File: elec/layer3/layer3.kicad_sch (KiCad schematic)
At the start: 46 parts, among them U1 CD74HC4067SM, U2 CD74HC4067SM, U3 TEENSY40, U4 4754, U5 113991054

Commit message: l3 almost done
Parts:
- removed U3: TEENSY40, layer2-pcb-footprints:TEENSY40, symbol layer2-pcb-symbols:TEENSY40
- added H1, H2, H3, H4: MountingHole, MountingHole:MountingHole_3.2mm_M3_DIN965_Pad, symbol Mechanical:MountingHole
- added J10, J4: Conn_01x05, Connector_JST:JST_XH_B5B-XH-A_1x05_P2.50mm_Vertical, symbol Connector_Generic:Conn_01x05
- added J8, J9: XT30PW-M, L3:AMASS_XT30PW-M, symbol layer1-pcb-symbols:XT30PW-M
- U1, U2: footprint CD74HC4067SM96G4:SOP65P780X200-24N -> L3:CD74HC4067SM
- U4: footprint IMU:MODULE_4754 -> L3:MODULE_4754
- U5: footprint Layer1_Symbol_Footprints:XiaoSeeedStudioEsp32 -> L3:XiaoSeeedStudioEsp32
- U6: footprint OPENMVM7V2:OPENMV_M7 -> L3:OPENMV_M7
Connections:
- net +3V3: now also J9.P
- net +5V: now also J8.P
- net GND: now also J10.5 (Pin_5), J4.5 (Pin_5), J8.N, J9.N
- net Mux Com (17-32): now also U5.1 (D0), U5.6 (D5)
- net RX (CAM): now also J4.3 (Pin_3)
- net RX(ESP32): now also J4.1 (Pin_1)
- net S0: now also U5.2 (D1)
- net S1: now also U5.3 (D2)
- net S2: now also U5.4 (D3)
- net S3: now also U5.5 (D4)
- net TX (CAM): now also J4.4 (Pin_4)
- net TX(ESP32): now also J4.2 (Pin_2)
- net RX(IMU) renamed SCL (IMU)
- net SCL (IMU): now also J10.1 (Pin_1)
- net TX(IMU) renamed SDA (IMU)
- net SDA (IMU): now also J10.2 (Pin_2)
- no-connect marks 50 -> 24

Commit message: l3 done
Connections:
- net Mux Com (17-32): no longer R33.2, U2.1 (COM), U5.6 (D5)
- new net Mux Com (1-16): R33.2, U2.1 (COM), U5.6 (D5)

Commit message: l3 touched
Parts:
- removed IR31, IR32: TSSP58038, OptoDevice:Vishay_MINICAST-3Pin, symbol Sensor_Proximity:TSSP58038
- added SW1, SW2, SW3, SW4: SW_SPDT_312, L3:SS12D00G3, symbol Switch:SW_SPDT_312
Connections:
- net IR31 is gone; now on net IR30: U1.17 (I14)
- net +3V3: now also SW1.3 (A), SW2.3 (A), SW3.3 (A), SW4.3 (A)
- net GND: now also SW1.2 (C), SW2.2 (C), SW3.2 (C), SW4.2 (C)
- net IR16: now also U1.9 (I0); no longer U2.16 (I15)
- net IR17: now also U1.8 (I1); no longer U1.9 (I0)
- net IR18: now also U1.7 (I2); no longer U1.8 (I1)
- net IR19: now also U1.6 (I3); no longer U1.7 (I2)
- net IR20: now also U1.5 (I4); no longer U1.6 (I3)
- net IR21: now also U1.4 (I5); no longer U1.5 (I4)
- net IR22: now also U1.3 (I6); no longer U1.4 (I5)
- net IR23: now also U1.2 (I7); no longer U1.3 (I6)
- net IR24: now also U1.23 (I8); no longer U1.2 (I7)
- net IR25: now also U1.22 (I9); no longer U1.23 (I8)
- net IR26: now also U1.21 (I10); no longer U1.22 (I9)
- net IR27: now also U1.20 (I11); no longer U1.21 (I10)
- net IR28: now also U1.19 (I12); no longer U1.20 (I11)
- net IR29: now also U1.18 (I13); no longer U1.19 (I12)
- net IR30: no longer U1.18 (I13)
- net Strat4: now reaches U5.10 (D9)
- net Strat4: now also SW4.1 (B)
- net Strat3: now reaches U5.9 (D8)
- net Strat3: now also SW3.1 (B)
- net IR32 renamed Strat2
- net Strat2: now also SW2.1 (B)
- new net Strat1: SW1.1 (B), U2.16 (I15)
- no-connect marks 24 -> 22

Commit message: l3 : edited schematics
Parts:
- removed IR15, IR30: TSSP58038, OptoDevice:Vishay_MINICAST-3Pin, symbol Sensor_Proximity:TSSP58038
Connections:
- net IR15 is gone; now on net Strat1: U2.17 (I14)
- net IR30 is gone; now on net Strat3: U1.17 (I14)
- net Strat1: no longer U2.16 (I15)
- net Strat2: now also U2.16 (I15); no longer U1.16 (I15)
- net Strat3: no longer U5.9 (D8)
- net Strat4: now also U1.16 (I15); no longer U5.10 (D9)
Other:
- moved on the sheet: IR29

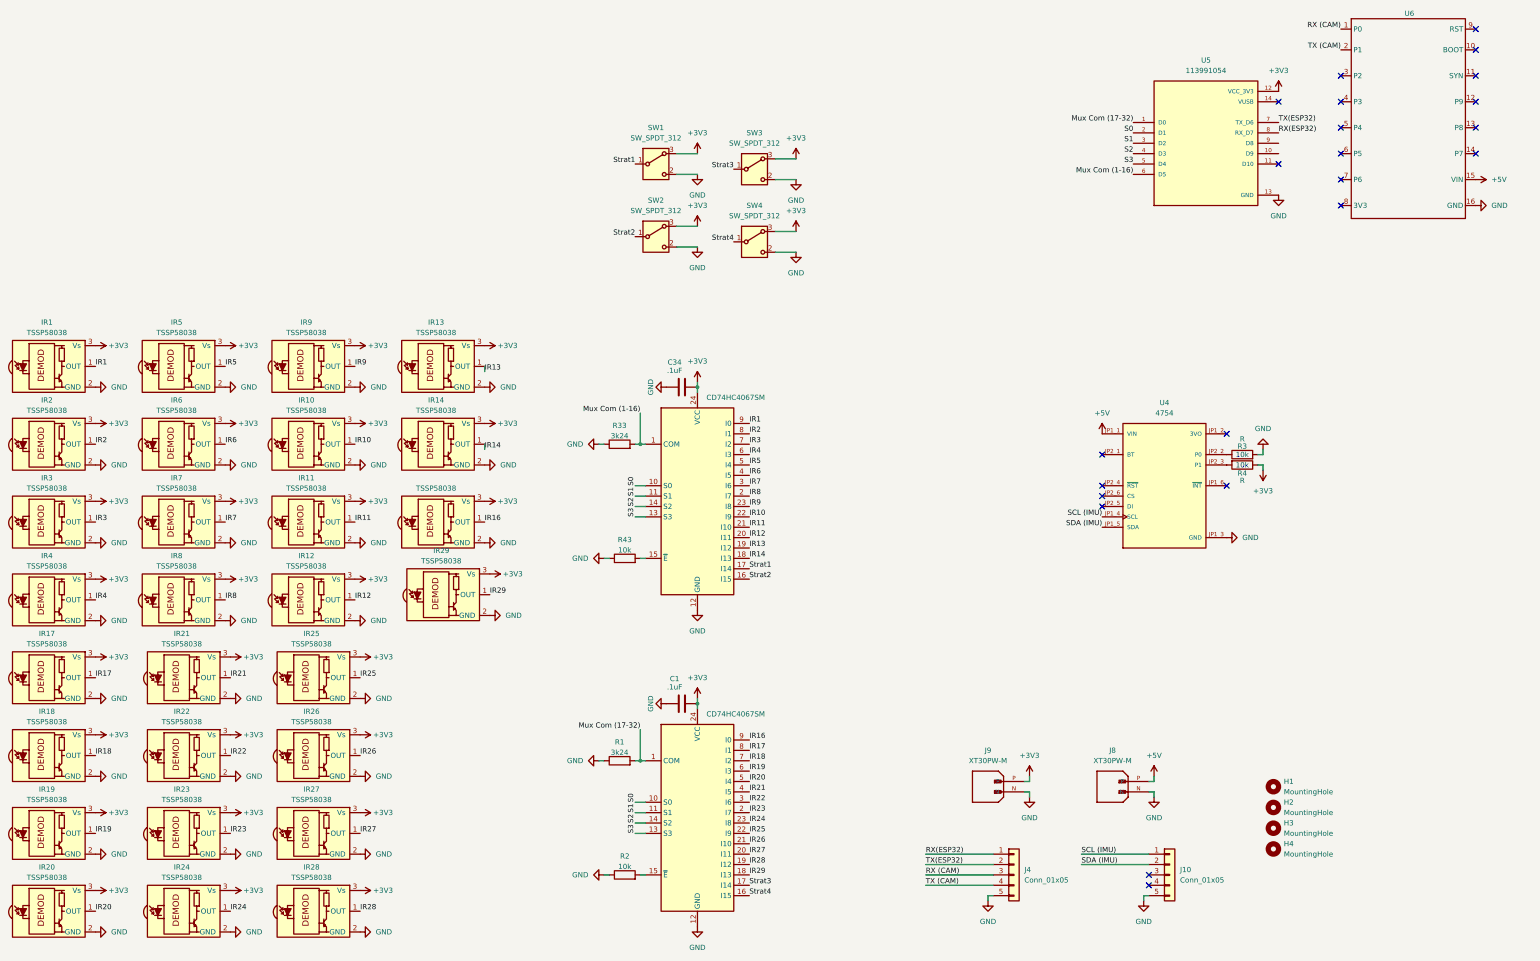
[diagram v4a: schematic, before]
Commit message: l3: changed gpio pins for esp32 to avoid 2 and 9
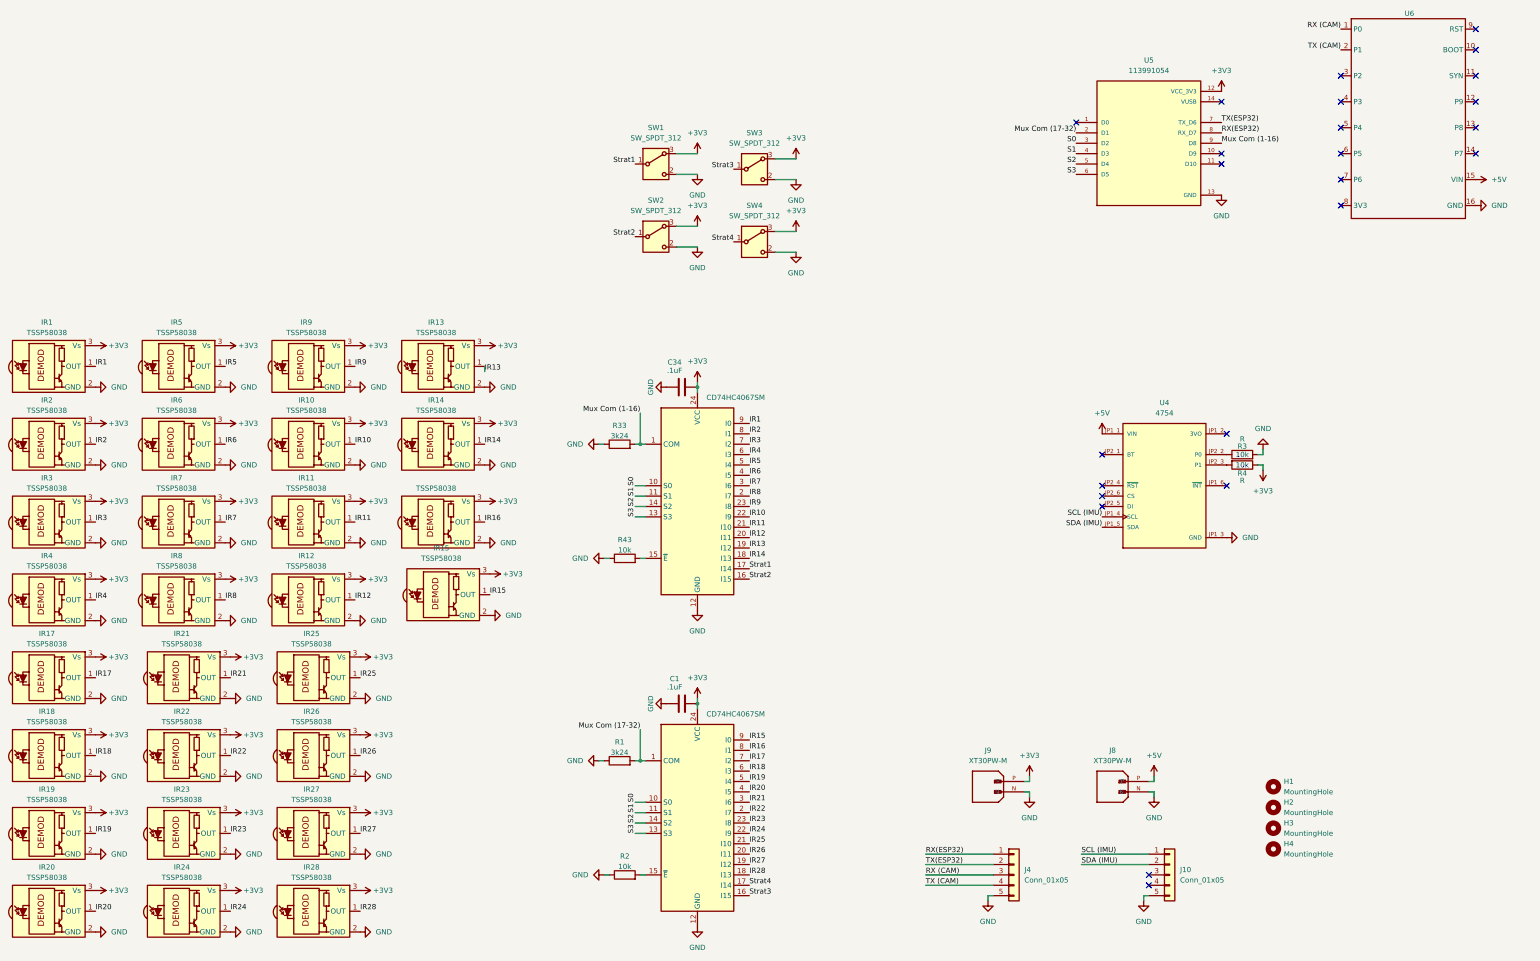
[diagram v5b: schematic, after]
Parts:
- renumbered IR29 to IR15
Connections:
- net IR16: now also U1.8 (I1); no longer U1.9 (I0)
- net IR17: now also U1.7 (I2); no longer U1.8 (I1)
- net IR18: now also U1.6 (I3); no longer U1.7 (I2)
- net IR19: now also U1.5 (I4); no longer U1.6 (I3)
- net IR20: now also U1.4 (I5); no longer U1.5 (I4)
- net IR21: now also U1.3 (I6); no longer U1.4 (I5)
- net IR22: now also U1.2 (I7); no longer U1.3 (I6)
- net IR23: now also U1.23 (I8); no longer U1.2 (I7)
- net IR24: now also U1.22 (I9); no longer U1.23 (I8)
- net IR25: now also U1.21 (I10); no longer U1.22 (I9)
- net IR26: now also U1.20 (I11); no longer U1.21 (I10)
- net IR27: now also U1.19 (I12); no longer U1.20 (I11)
- net IR28: now also U1.18 (I13); no longer U1.19 (I12)
- net Mux Com (1-16): now also U5.9 (D8); no longer U5.6 (D5)
- net Mux Com (17-32): now also U5.2 (D1); no longer U5.1 (D0)
- net S0: now also U5.3 (D2); no longer U5.2 (D1)
- net S1: now also U5.4 (D3); no longer U5.3 (D2)
- net S2: now also U5.5 (D4); no longer U5.4 (D3)
- net S3: now also U5.6 (D5); no longer U5.5 (D4)
- net Strat3: now also U1.16 (I15); no longer U1.17 (I14)
- net Strat4: now also U1.17 (I14); no longer U1.16 (I15)
- net IR29 renamed IR15
- net IR15: now also U1.9 (I0); no longer U1.18 (I13)
- no-connect marks 22 -> 24
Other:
- moved on the sheet: U5

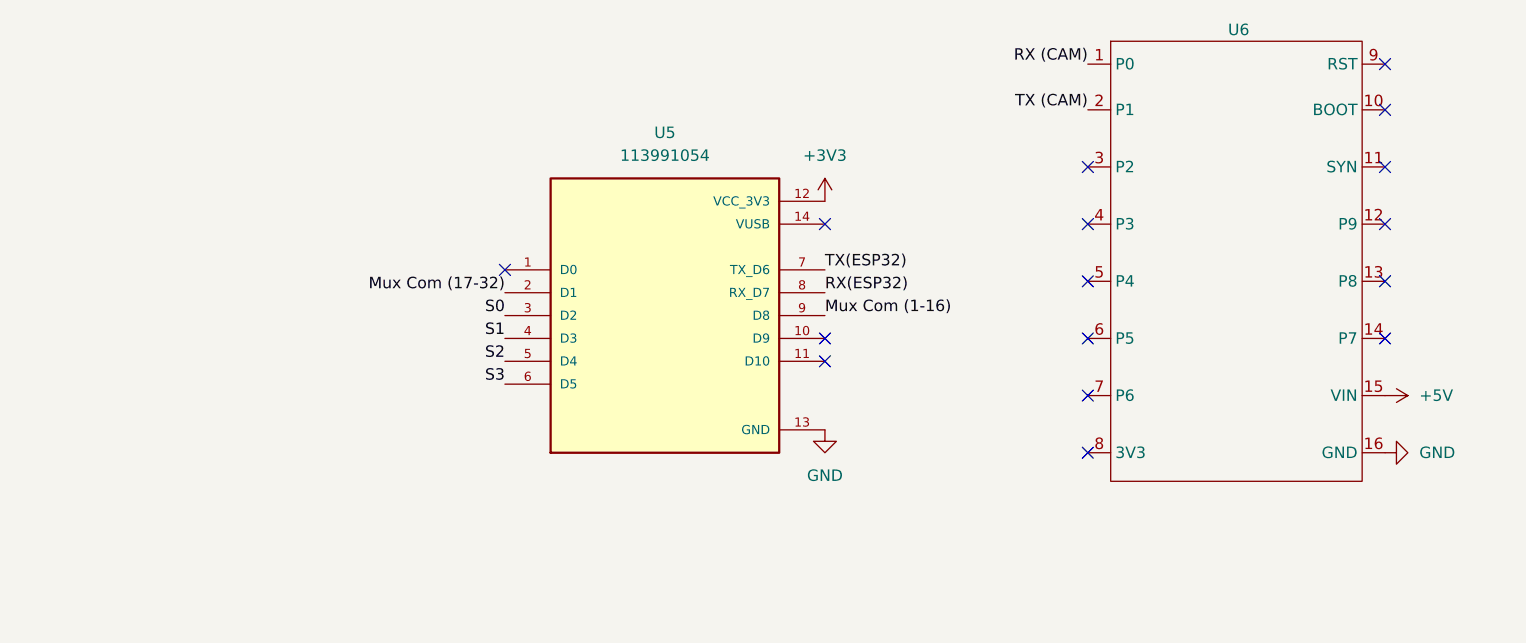
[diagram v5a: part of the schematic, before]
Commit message: added res and cap
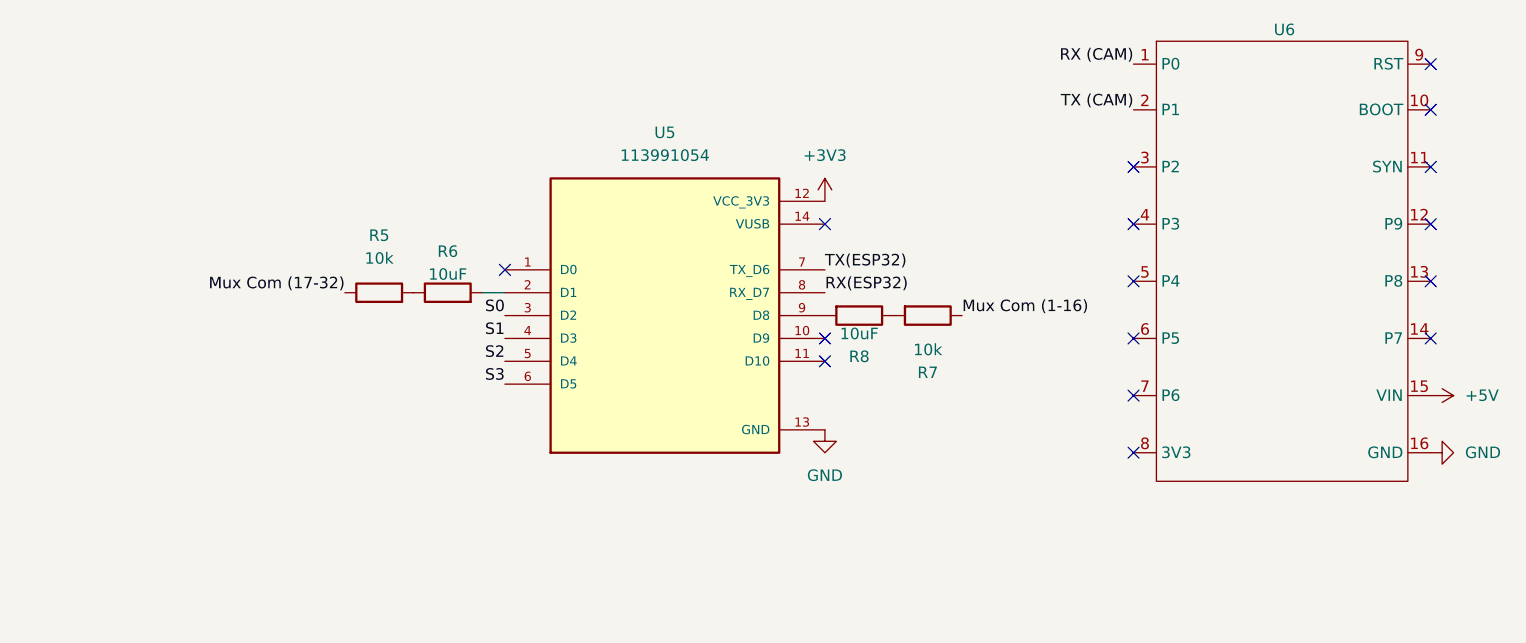
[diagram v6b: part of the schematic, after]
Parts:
- added R5, R7: 10k, Resistor_SMD:R_0603_1608Metric, symbol Device:R
- added R6, R8: 10uF, Resistor_SMD:R_0603_1608Metric, symbol Device:R
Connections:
- net Mux Com (1-16): now also R7.1; no longer U5.9 (D8)
- net Mux Com (17-32): now also R5.1; no longer U5.2 (D1)
- new net: R5.2, R6.1
- new net: R6.2, U5.2 (D1)
- new net: R8.2, U5.9 (D8)
- new net: R7.2, R8.1
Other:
- moved on the sheet: U6

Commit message: l3 : sw change
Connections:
- net GND: now also SW1.1 (B), SW2.1 (B), SW3.1 (B), SW4.1 (B); no longer SW1.2 (C), SW2.2 (C), SW3.2 (C), SW4.2 (C)
- net Strat1: now also SW1.2 (C); no longer SW1.1 (B)
- net Strat2: now also SW2.2 (C); no longer SW2.1 (B)
- net Strat3: now also SW3.2 (C); no longer SW3.1 (B)
- net Strat4: now also SW4.2 (C); no longer SW4.1 (B)
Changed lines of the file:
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@@
 	)
 	(label "Strat1"
-		(at 187.96 63.5 180)
+		(at 203.2 66.04 0)
 		(effects
 			(font
 				(size 1.27 1.27)
 			)
-			(justify right bottom)
+			(justify left bottom)
 		)
 	)
@@
 	)
 	(label "Strat2"
-		(at 187.96 81.28 180)
+		(at 203.2 83.82 0)
 		(effects
 			(font
 				(size 1.27 1.27)
 			)
-			(justify right bottom)
+			(justify left bottom)
 		)
 	)
@@
 	)
 	(label "Strat4"
-		(at 212.09 82.55 180)
+		(at 227.33 85.09 0)
 		(effects
 			(font
 				(size 1.27 1.27)
 			)
-			(justify right bottom)
+			(justify left bottom)
 		)
 	)
@@
 	)
 	(label "Strat3"
-		(at 212.09 64.77 180)
+		(at 227.33 67.31 0)
 		(effects
 			(font
 				(size 1.27 1.27)
 			)
-			(justify right bottom)
+			(justify left bottom)
 		)
 	)
@@
 	(symbol
 		(lib_id "power:GND")
-		(at 203.2 83.82 0)
+		(at 187.96 81.28 0)
 		(unit 1)
 		(exclude_from_sim no)
@@
 		(fields_autoplaced yes)
 		(property "Reference" "#PWR092"
-			(at 203.2 90.17 0)
+			(at 187.96 87.63 0)
 			(effects
 				(font
@@
 		)
 		(property "Value" "GND"
-			(at 203.2 88.9 0)
+			(at 187.96 86.36 0)
 			(effects
 				(font
@@
 		)
 		(property "Footprint" ""
-			(at 203.2 83.82 0)
+			(at 187.96 81.28 0)
 			(effects
 				(font
@@
 		)
 		(property "Datasheet" ""
-			(at 203.2 83.82 0)
+			(at 187.96 81.28 0)
 			(effects
 				(font
@@
 		)
 		(property "Description" "Power symbol creates a global label with name \"GND\" , ground"
-			(at 203.2 83.82 0)
+			(at 187.96 81.28 0)
 			(effects
 				(font
@@
 	(symbol
 		(lib_id "power:GND")
-		(at 227.33 67.31 0)
+		(at 212.09 64.77 0)
 		(unit 1)
 		(exclude_from_sim no)
@@
 		(fields_autoplaced yes)
 		(property "Reference" "#PWR094"
-			(at 227.33 73.66 0)
+			(at 212.09 71.12 0)
 			(effects
 				(font
@@
 		)
 		(property "Value" "GND"
-			(at 227.33 72.39 0)
+			(at 212.09 69.85 0)
 			(effects
 				(font
@@
 		)
 		(property "Footprint" ""
-			(at 227.33 67.31 0)
+			(at 212.09 64.77 0)
 			(effects
 				(font
@@
 		)
 		(property "Datasheet" ""
-			(at 227.33 67.31 0)
+			(at 212.09 64.77 0)
 			(effects
 				(font
@@
 		)
 		(property "Description" "Power symbol creates a global label with name \"GND\" , ground"
-			(at 227.33 67.31 0)
+			(at 212.09 64.77 0)
 			(effects
 				(font
@@
 	(symbol
 		(lib_id "power:GND")
-		(at 227.33 85.09 0)
+		(at 212.09 82.55 0)
 		(unit 1)
 		(exclude_from_sim no)
@@
 		(fields_autoplaced yes)
 		(property "Reference" "#PWR096"
-			(at 227.33 91.44 0)
+			(at 212.09 88.9 0)
 			(effects
 				(font
@@
 		)
 		(property "Value" "GND"
-			(at 227.33 90.17 0)
+			(at 212.09 87.63 0)
 			(effects
 				(font
@@
 		)
 		(property "Footprint" ""
-			(at 227.33 85.09 0)
+			(at 212.09 82.55 0)
 			(effects
 				(font
@@
 		)
 		(property "Datasheet" ""
-			(at 227.33 85.09 0)
+			(at 212.09 82.55 0)
 			(effects
 				(font
@@
 		)
 		(property "Description" "Power symbol creates a global label with name \"GND\" , ground"
-			(at 227.33 85.09 0)
+			(at 212.09 82.55 0)
 			(effects
 				(font
@@
 	(symbol
 		(lib_id "power:GND")
-		(at 203.2 66.04 0)
+		(at 187.96 63.5 0)
 		(unit 1)
 		(exclude_from_sim no)
@@
 		(on_board yes)
 		(dnp no)
-		(fields_autoplaced yes)
 		(property "Reference" "#PWR090"
-			(at 203.2 72.39 0)
+			(at 187.96 69.85 0)
 			(effects
 				(font
@@
 		)
 		(property "Value" "GND"
-			(at 203.2 71.12 0)
+			(at 185.928 67.818 0)
 			(effects
 				(font
 					(size 1.27 1.27)
 				)
+				(justify left)
 			)
 		)
 		(property "Footprint" ""
-			(at 203.2 66.04 0)
+			(at 187.96 63.5 0)
 			(effects
 				(font
@@
 		)
 		(property "Datasheet" ""
-			(at 203.2 66.04 0)
+			(at 187.96 63.5 0)
 			(effects
 				(font
@@
 		)
 		(property "Description" "Power symbol creates a global label with name \"GND\" , ground"
-			(at 203.2 66.04 0)
+			(at 187.96 63.5 0)
 			(effects
 				(font

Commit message: l3 : done
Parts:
- J8, J9: footprint L3:AMASS_XT30PW-M -> Connector_AMASS:AMASS_XT30UPB-M_1x02_P5.0mm_Vertical
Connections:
- net +3V3: no longer U5.12 (VCC_3V3)
- net +5V: now also U5.14 (VUSB)
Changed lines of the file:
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@@
 	)
 	(no_connect
+		(at 331.47 45.72)
+	)
+	(no_connect
 		(at 302.26 144.78)
 	)
@@
 	)
 	(no_connect
-		(at 331.47 48.26)
-	)
-	(no_connect
 		(at 313.69 237.49)
 	)
@@
 	)
 	(symbol
+		(lib_id "power:+5V")
+		(at 331.47 48.26 270)
+		(unit 1)
+		(exclude_from_sim no)
+		(in_bom yes)
+		(on_board yes)
+		(dnp no)
+		(fields_autoplaced yes)
+		(property "Reference" "#PWR034"
+			(at 327.66 48.26 0)
+			(effects
+				(font
+					(size 1.27 1.27)
+				)
+				(hide yes)
+			)
+		)
+		(property "Value" "+5V"
+			(at 335.28 48.2599 90)
+			(effects
+				(font
+					(size 1.27 1.27)
+				)
+				(justify left)
+			)
+		)
+		(property "Footprint" ""
+			(at 331.47 48.26 0)
+			(effects
+				(font
+					(size 1.27 1.27)
+				)
+				(hide yes)
+			)
+		)
+		(property "Datasheet" ""
+			(at 331.47 48.26 0)
+			(effects
+				(font
+					(size 1.27 1.27)
+				)
+				(hide yes)
+			)
+		)
+		(property "Description" "Power symbol creates a global label with name \"+5V\""
+			(at 331.47 48.26 0)
+			(effects
+				(font
+					(size 1.27 1.27)
+				)
+				(hide yes)
+			)
+		)
+		(pin "1"
+		)
+		(instances
+			(project ""
+				(path "/6d022762-18f1-42b1-b82f-80e730c6e13f"
+					(reference "#PWR034")
+					(unit 1)
+				)
+			)
+		)
+	)
+	(symbol
 		(lib_id "Sensor_Proximity:TSSP58038")
 		(at 110.49 246.38 0)
@@
 			)
 		)
-		(property "Footprint" "L3:AMASS_XT30PW-M"
+		(property "Footprint" "Connector_AMASS:AMASS_XT30UPB-M_1x02_P5.0mm_Vertical"
 			(at 308.61 214.63 0)
 			(effects
@@
 			)
 		)
-		(property "Footprint" "L3:AMASS_XT30PW-M"
+		(property "Footprint" "Connector_AMASS:AMASS_XT30UPB-M_1x02_P5.0mm_Vertical"
 			(at 278.13 214.63 0)
 			(effects
@@
 					(unit 1)
 				)
-			)
-		)
-	)
-	(symbol
-		(lib_id "power:+3V3")
-		(at 331.47 45.72 0)
-		(unit 1)
-		(exclude_from_sim no)
-		(in_bom yes)
-		(on_board yes)
-		(dnp no)
-		(fields_autoplaced yes)
-		(property "Reference" "#PWR084"
-			(at 331.47 49.53 0)
-			(effects
-				(font
-					(size 1.27 1.27)
-				)
-				(hide yes)
-			)
-		)
-		(property "Value" "+3V3"
-			(at 331.47 40.64 0)
-			(effects
-				(font
-					(size 1.27 1.27)
-				)
-			)
-		)
-		(property "Footprint" ""
-			(at 331.47 45.72 0)
-			(effects
-				(font
-					(size 1.27 1.27)
-				)
-				(hide yes)
-			)
-		)
-		(property "Datasheet" ""
-			(at 331.47 45.72 0)
-			(effects
-				(font
-					(size 1.27 1.27)
-				)
-				(hide yes)
-			)
-		)
-		(property "Description" "Power symbol creates a global label with name \"+3V3\""
-			(at 331.47 45.72 0)
-			(effects
-				(font
-					(size 1.27 1.27)
-				)
-				(hide yes)
-			)
-		)
-		(pin "1"
-		)
-		(instances
-			(project ""
-				(path "/6d022762-18f1-42b1-b82f-80e730c6e13f"
-					(reference "#PWR084")
-					(unit 1)
-				)
